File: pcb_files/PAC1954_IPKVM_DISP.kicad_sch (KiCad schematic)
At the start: 11 parts, among them U25 PAC1954T-E_4MX

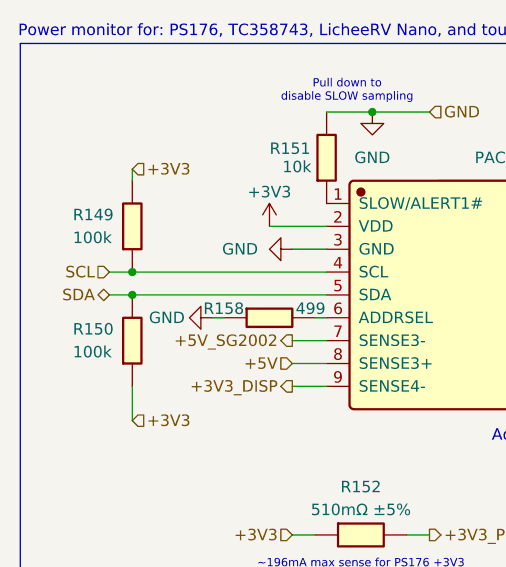
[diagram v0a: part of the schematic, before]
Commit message: Basic Function Review/Documentation for MCP9808
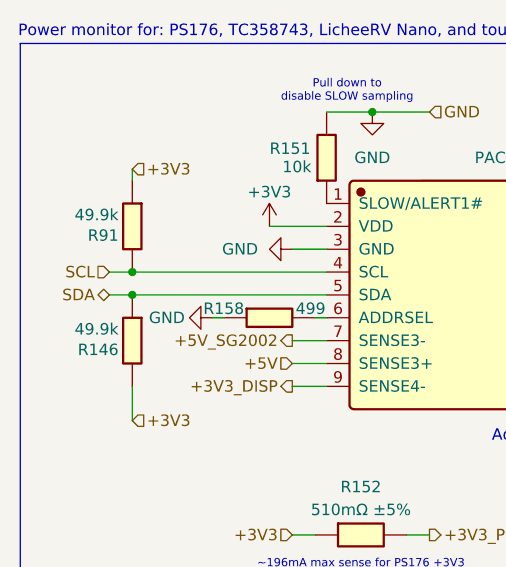
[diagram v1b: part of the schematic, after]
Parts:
- removed R149, R150: 100k, Resistor_SMD:R_0402_1005Metric, symbol JLCImport:0402WGF1003TCE
- added R146, R91: 49.9k, Resistor_SMD:R_0402_1005Metric, symbol JLCImport:RMS04FT4992
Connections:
- net +3V3: now also R146.2, R91.1
- net SCL: now also R91.2
- net SDA: now also R146.1

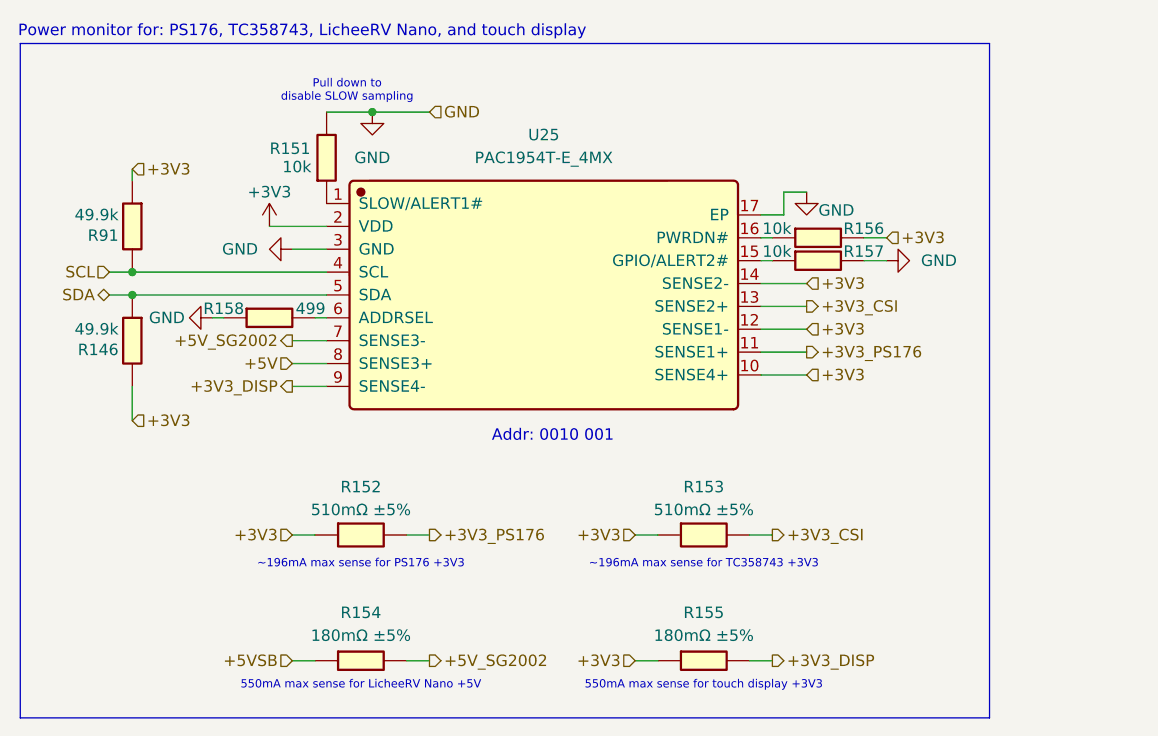
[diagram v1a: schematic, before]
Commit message: Switched PAC1954 to SLOW mode to save power
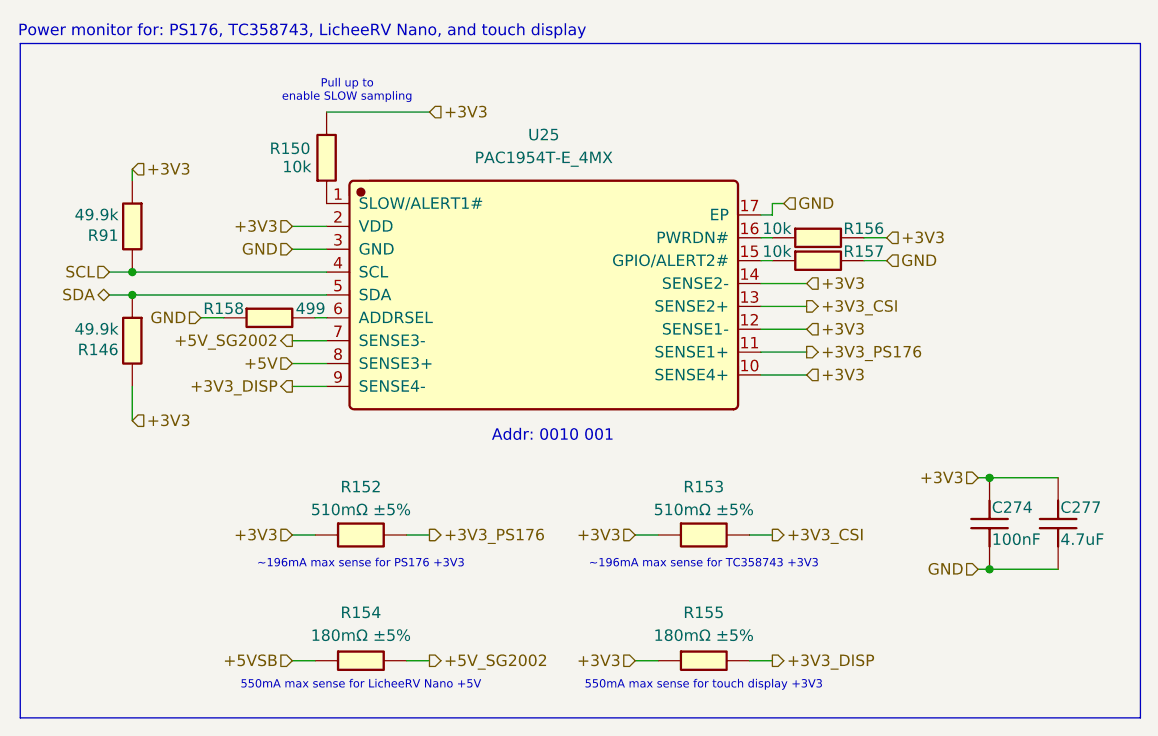
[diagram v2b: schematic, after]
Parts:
- removed R151: 10k, Resistor_SMD:R_0402_1005Metric, symbol JLCImport:0402WGF1002TCE
- added C274: 100nF, Capacitor_SMD:C_0402_1005Metric, symbol JLCImport:CL05B104KB54PNC
- added C277: 4.7uF, Capacitor_SMD:C_0402_1005Metric, symbol JLCImport:CL05A475MP5NRNC
- added R150: 10k, Resistor_SMD:R_0402_1005Metric, symbol JLCImport:0402WGF1002TCE
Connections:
- net +3V3: now also C274.2, C277.2, R150.2
- net GND: now also C274.1, C277.1
- net at U25.1 (SLOW/ALERT1#): now also R150.1
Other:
- note added: "Pull up to enable SLOW sampling"
- note removed: "Pull down to disable SLOW sampling"

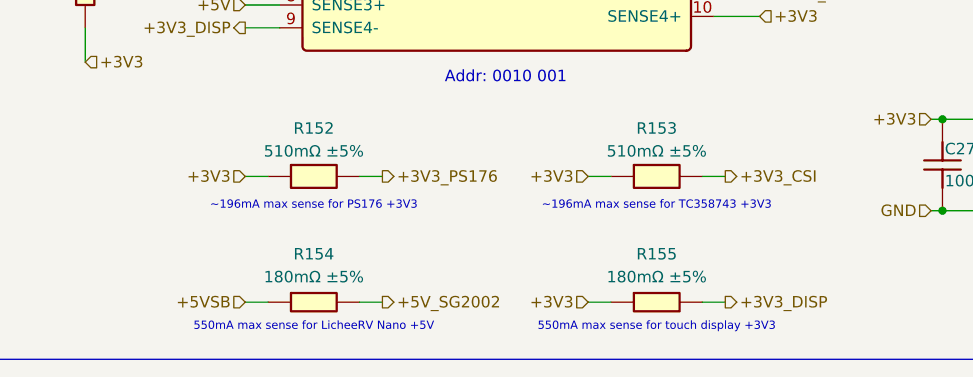
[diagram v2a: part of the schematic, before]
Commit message: Basic Function Review/Documentation for PAC1954 for IPKVM and Display
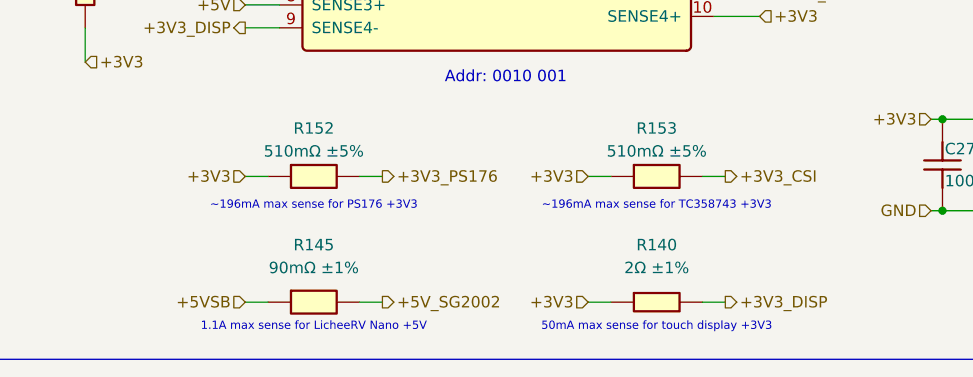
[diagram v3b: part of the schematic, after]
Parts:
- removed R154, R155: 180mΩ ±5%, Resistor_SMD:R_0508_1220Metric, symbol JLCImport:LTR10EVHJLR18
- added R140: 2Ω ±1%, Resistor_SMD:R_1206_3216Metric, symbol JLCImport:1206W3J010LT5E
- added R145: 90mΩ ±1%, Resistor_SMD:R_2512_6332Metric, symbol JLCImport:JER2512F2R100
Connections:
- net +3V3: now also R140.1
- net +3V3_DISP: now also R140.2
- net +5VSB: now also R145.1
- net +5V_SG2002: now also R145.2
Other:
- note added: "1.1A max sense for LicheeRV Nano +5V"
- note added: "50mA max sense for touch display +3V3"
- note removed: "550mA max sense for LicheeRV Nano +5V"
- note removed: "550mA max sense for touch display +3V3"
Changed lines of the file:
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@@
 		)
 	)
-	(text "550mA max sense for touch display +3V3"
+	(text "50mA max sense for touch display +3V3"
 		(exclude_from_sim no)
 		(at 92.71 89.154 0)
@@
 		)
 	)
-	(text "550mA max sense for LicheeRV Nano +5V"
+	(text "1.1A max sense for LicheeRV Nano +5V"
 		(exclude_from_sim no)
 		(at 54.61 89.154 0)
@@
 			)
 			(justify left)
+		)
+	)
+	(symbol
+		(lib_id "JLCImport:1206W3J010LT5E")
+		(at 92.71 86.36 0)
+		(unit 1)
+		(body_style 1)
+		(exclude_from_sim no)
+		(in_bom yes)
+		(on_board yes)
+		(in_pos_files yes)
+		(dnp no)
+		(fields_autoplaced yes)
+		(property "Reference" "R140"
+			(at 92.71 80.01 0)
+			(show_name no)
+			(do_not_autoplace no)
+			(effects
+				(font
+					(size 1.27 1.27)
+				)
+			)
+		)
+		(property "Value" "2Ω ±1%"
+			(at 92.71 82.55 0)
+			(show_name no)
+			(do_not_autoplace no)
+			(effects
+				(font
+					(size 1.27 1.27)
+				)
+			)
+		)
+		(property "Footprint" "Resistor_SMD:R_1206_3216Metric"
+			(at 92.71 86.36 0)
+			(hide yes)
+			(show_name no)
+			(do_not_autoplace no)
+			(effects
+				(font
+					(size 1.27 1.27)
+				)
+			)
+		)
+		(property "Datasheet" ""
+			(at 92.71 86.36 0)
+			(hide yes)
+			(show_name no)
+			(do_not_autoplace no)
+			(effects
+				(font
+					(size 1.27 1.27)
+				)
+			)
+		)
+		(property "Description" "2Ω 200V 500mW Thick Film Resistor  ±1% 1206 Chip Resistor - Surface Mount ROHS"
+			(at 92.71 86.36 0)
+			(hide yes)
+			(show_name no)
+			(do_not_autoplace no)
+			(effects
+				(font
+					(size 1.27 1.27)
+				)
+			)
+		)
+		(property "LCSC" "C54102244"
+			(at 92.71 86.36 0)
+			(hide yes)
+			(show_name no)
+			(do_not_autoplace no)
+			(effects
+				(font
+					(size 1.27 1.27)
+				)
+			)
+		)
+		(property "Manufacturer" "FOJAN"
+			(at 92.71 86.36 0)
+			(hide yes)
+			(show_name no)
+			(do_not_autoplace no)
+			(effects
+				(font
+					(size 1.27 1.27)
+				)
+			)
+		)
+		(property "Manufacturer Part" "FRP1206F2R00TS"
+			(at 92.71 86.36 0)
+			(hide yes)
+			(show_name no)
+			(do_not_autoplace no)
+			(effects
+				(font
+					(size 1.27 1.27)
+				)
+			)
+		)
+		(pin "1"
+		)
+		(pin "2"
+		)
+		(instances
+			(project "serverv2_backplane"
+				(path "/d38d6818-cf53-410d-afa3-a75a85b7c05a/f2e967c0-ce90-4cb8-9de5-e046db142ae2"
+					(reference "R140")
+					(unit 1)
+				)
+			)
 		)
 	)
@@
 				(path "/d38d6818-cf53-410d-afa3-a75a85b7c05a/f2e967c0-ce90-4cb8-9de5-e046db142ae2"
 					(reference "R156")
+					(unit 1)
+				)
+			)
+		)
+	)
+	(symbol
+		(lib_id "JLCImport:JER2512F2R100")
+		(at 54.61 86.36 0)
+		(unit 1)
+		(body_style 1)
+		(exclude_from_sim no)
+		(in_bom yes)
+		(on_board yes)
+		(in_pos_files yes)
+		(dnp no)
+		(fields_autoplaced yes)
+		(property "Reference" "R145"
+			(at 54.61 80.01 0)
+			(show_name no)
+			(do_not_autoplace no)
+			(effects
+				(font
+					(size 1.27 1.27)
+				)
+			)
+		)
+		(property "Value" "90mΩ ±1%"
+			(at 54.61 82.55 0)
+			(show_name no)
+			(do_not_autoplace no)
+			(effects
+				(font
+					(size 1.27 1.27)
+				)
+			)
+		)
+		(property "Footprint" "Resistor_SMD:R_2512_6332Metric"
+			(at 54.61 86.36 0)
+			(hide yes)
+			(show_name no)
+			(do_not_autoplace no)
+			(effects
+				(font
+					(size 1.27 1.27)
+				)
+			)
+		)
+		(property "Datasheet" ""
+			(at 54.61 86.36 0)
+			(hide yes)
+			(show_name no)
+			(do_not_autoplace no)
+			(effects
+				(font
+					(size 1.27 1.27)
+				)
+			)
+		)
+		(property "Description" "90mΩ 3W Current Sense Resistor SMD ±1% ±50ppm/℃ 2512 Current Sense Resistors / Shunt Resistors ROHS"
+			(at 54.61 86.36 0)
+			(hide yes)
+			(show_name no)
+			(do_not_autoplace no)
+			(effects
+				(font
+					(size 1.27 1.27)
+				)
+			)
+		)
+		(property "LCSC" "C49164915"
+			(at 54.61 86.36 0)
+			(hide yes)
+			(show_name no)
+			(do_not_autoplace no)
+			(effects
+				(font
+					(size 1.27 1.27)
+				)
+			)
+		)
+		(property "Manufacturer" "JIERR"
+			(at 54.61 86.36 0)
+			(hide yes)
+			(show_name no)
+			(do_not_autoplace no)
+			(effects
+				(font
+					(size 1.27 1.27)
+				)
+			)
+		)
+		(property "Manufacturer Part" "JER2512F3R090"
+			(at 54.61 86.36 0)
+			(hide yes)
+			(show_name no)
+			(do_not_autoplace no)
+			(effects
+				(font
+					(size 1.27 1.27)
+				)
+			)
+		)
+		(pin "1"
+		)
+		(pin "2"
+		)
+		(instances
+			(project "serverv2_backplane"
+				(path "/d38d6818-cf53-410d-afa3-a75a85b7c05a/f2e967c0-ce90-4cb8-9de5-e046db142ae2"
+					(reference "R145")
 					(unit 1)
 				)
@@
 					(unit 1)
 				)
-			)
-		)
-	)
-	(symbol
-		(lib_id "JLCImport:LTR10EVHJLR18")
-		(at 54.61 86.36 0)
-		(unit 1)
-		(body_style 1)
-		(exclude_from_sim no)
-		(in_bom yes)
-		(on_board yes)
-		(in_pos_files yes)
-		(dnp no)
-		(property "Reference" "R154"
-			(at 54.61 81.026 0)
-			(show_name no)
-			(do_not_autoplace no)
-			(effects
-				(font
-					(size 1.27 1.27)
-				)
-			)
-		)
-		(property "Value" "180mΩ ±5%"
-			(at 54.61 83.566 0)
-			(show_name no)
-			(do_not_autoplace no)
-			(effects
-				(font
-					(size 1.27 1.27)
-				)
-			)
-		)
-		(property "Footprint" "Resistor_SMD:R_0508_1220Metric"
-			(at 54.61 86.36 0)
-			(hide yes)
-			(show_name no)
-			(do_not_autoplace no)
-			(effects
-				(font
-					(size 1.27 1.27)
-				)
-			)
-		)
-		(property "Datasheet" "https://www.lcsc.com/datasheet/lcsc_datasheet_2304140030_ROHM-Semicon-LTR10EVHJLR18_C253348.pdf"
-			(at 54.61 86.36 0)
-			(hide yes)
-			(show_name no)
-			(do_not_autoplace no)
-			(effects
-				(font
-					(size 1.27 1.27)
-				)
-			)
-		)
-		(property "Description" "180mΩ 500mW SMD ±150ppm/℃ ±5% 0805 Current Sense Resistors / Shunt Resistors ROHS"
-			(at 54.61 86.36 0)
-			(hide yes)
-			(show_name no)
-			(do_not_autoplace no)
-			(effects
-				(font
-					(size 1.27 1.27)
-				)
-			)
-		)
-		(property "LCSC" "C253348"
-			(at 54.61 86.36 0)
-			(hide yes)
-			(show_name no)
-			(do_not_autoplace no)
-			(effects
-				(font
-					(size 1.27 1.27)
-				)
-			)
-		)
-		(property "Manufacturer" "ROHM Semicon"
-			(at 54.61 86.36 0)
-			(hide yes)
-			(show_name no)
-			(do_not_autoplace no)
-			(effects
-				(font
-					(size 1.27 1.27)
-				)
-			)
-		)
-		(property "Manufacturer Part" "LTR10EVHJLR18"
-			(at 54.61 86.36 0)
-			(hide yes)
-			(show_name no)
-			(do_not_autoplace no)
-			(effects
-				(font
-					(size 1.27 1.27)
-				)
-			)
-		)
-		(pin "1"
-		)
-		(pin "2"
-		)
-		(instances
-			(project "serverv2_backplane"
-				(path "/d38d6818-cf53-410d-afa3-a75a85b7c05a/f2e967c0-ce90-4cb8-9de5-e046db142ae2"
-					(reference "R154")
-					(unit 1)
-				)
-			)
-		)
-	)
-	(symbol
-		(lib_id "JLCImport:LTR10EVHJLR18")
-		(at 92.71 86.36 0)
-		(unit 1)
-		(body_style 1)
-		(exclude_from_sim no)
-		(in_bom yes)
-		(on_board yes)
-		(in_pos_files yes)
-		(dnp no)
-		(property "Reference" "R155"
-			(at 92.71 81.026 0)
-			(show_name no)
-			(do_not_autoplace no)
-			(effects
-				(font
-					(size 1.27 1.27)
-				)
-			)
-		)
-		(property "Value" "180mΩ ±5%"
-			(at 92.71 83.566 0)
-			(show_name no)
-			(do_not_autoplace no)
-			(effects
-				(font
-					(size 1.27 1.27)
-				)
-			)
-		)
-		(property "Footprint" "Resistor_SMD:R_0508_1220Metric"
-			(at 92.71 86.36 0)
-			(hide yes)
-			(show_name no)
-			(do_not_autoplace no)
-			(effects
-				(font
-					(size 1.27 1.27)
-				)
-			)
-		)
-		(property "Datasheet" "https://www.lcsc.com/datasheet/lcsc_datasheet_2304140030_ROHM-Semicon-LTR10EVHJLR18_C253348.pdf"
-			(at 92.71 86.36 0)
-			(hide yes)
-			(show_name no)
-			(do_not_autoplace no)
-			(effects
-				(font
-					(size 1.27 1.27)
-				)
-			)
-		)
-		(property "Description" "180mΩ 500mW SMD ±150ppm/℃ ±5% 0805 Current Sense Resistors / Shunt Resistors ROHS"
-			(at 92.71 86.36 0)
-			(hide yes)
-			(show_name no)
-			(do_not_autoplace no)
-			(effects
-				(font
-					(size 1.27 1.27)
-				)
-			)
-		)
-		(property "LCSC" "C253348"
-			(at 92.71 86.36 0)
-			(hide yes)
-			(show_name no)
-			(do_not_autoplace no)
-			(effects
-				(font
-					(size 1.27 1.27)
-				)
-			)
-		)
-		(property "Manufacturer" "ROHM Semicon"
-			(at 92.71 86.36 0)
-			(hide yes)
-			(show_name no)
-			(do_not_autoplace no)
-			(effects
-				(font
-					(size 1.27 1.27)
-				)
-			)
-		)
-		(property "Manufacturer Part" "LTR10EVHJLR18"
-			(at 92.71 86.36 0)
-			(hide yes)
-			(show_name no)
-			(do_not_autoplace no)
-			(effects
-				(font
-					(size 1.27 1.27)
-				)
-			)
-		)
-		(pin "1"
-		)
-		(pin "2"
-		)
-		(instances
-			(project "serverv2_backplane"
-				(path "/d38d6818-cf53-410d-afa3-a75a85b7c05a/f2e967c0-ce90-4cb8-9de5-e046db142ae2"
-					(reference "R155")
-					(unit 1)
-				)
